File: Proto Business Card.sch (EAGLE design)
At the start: 551 parts

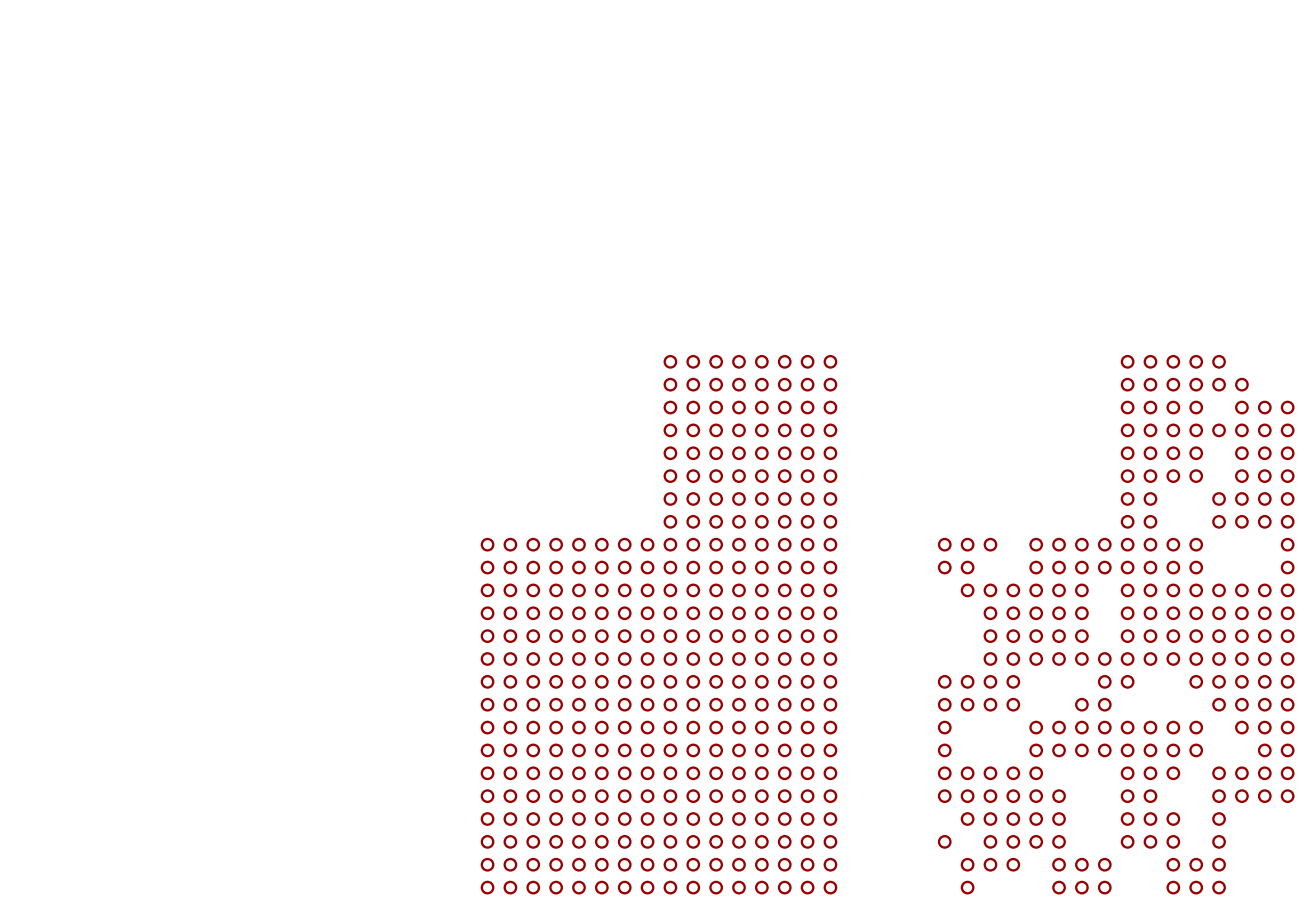
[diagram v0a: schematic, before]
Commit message: Text is now on, and the grid is complete. Still missing example layers on the back
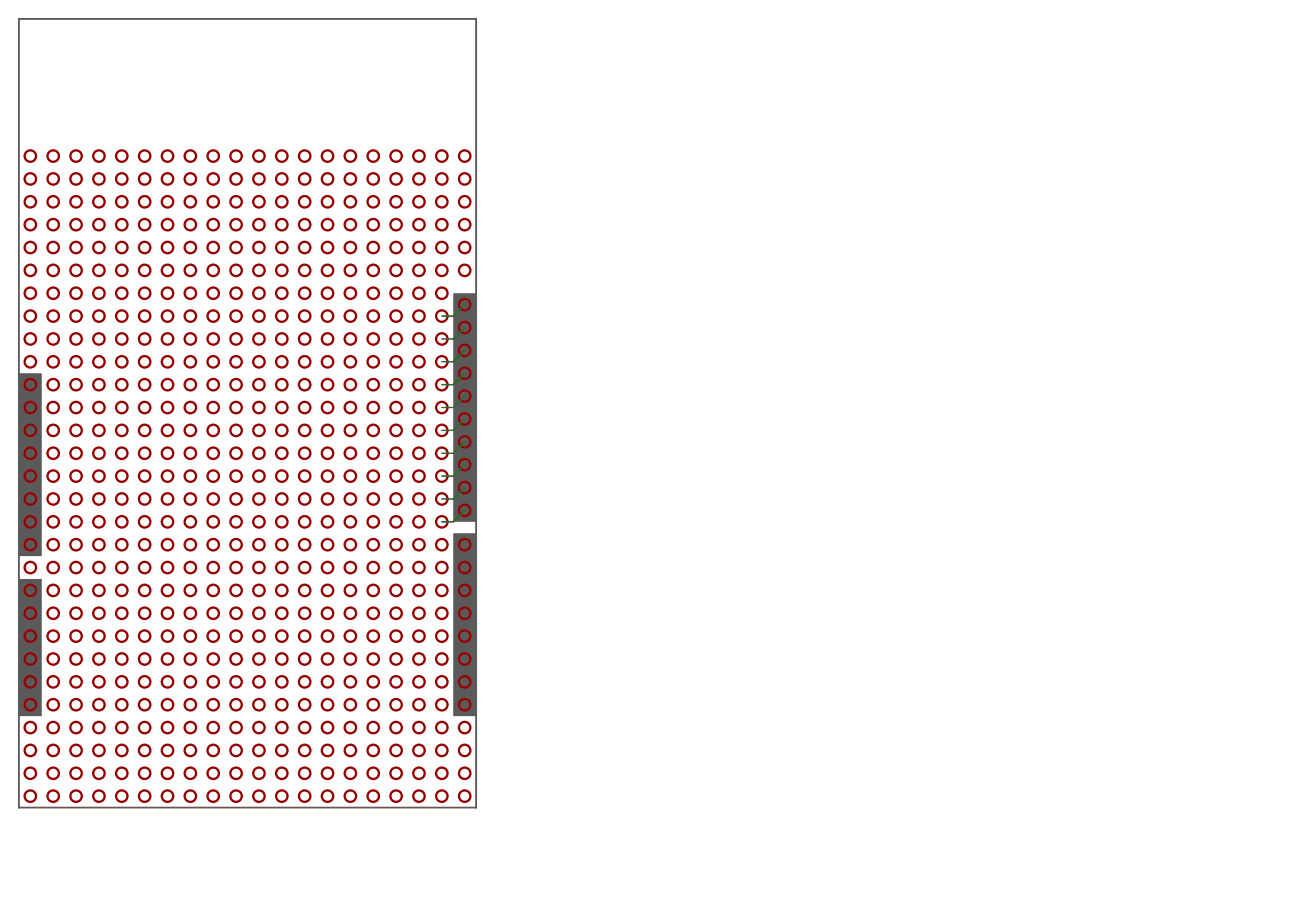
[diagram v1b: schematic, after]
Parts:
- removed U$576, U$577, U$578, U$579, U$580, U$581, U$582, U$583, U$584, U$589, U$596, U$597, U$598, U$599, U$600, U$601, U$602, U$603, U$604, U$605, U$606, U$607, U$608, U$609, U$610, U$611, U$612, U$613, U$614, U$621, U$622, U$623, U$624, U$625, U$626, U$627, U$628, U$629, U$630, U$631, U$632, U$633, U$634, U$635, U$636, U$637, U$638, U$639: VIA.4-4, flowerpad:VIA.4-4
- added U$100, U$148, U$149, U$74, U$75, U$95, U$96, U$97, U$98, U$99: VIA.NONE, flowerpad:VIA.NONE
- added U$120, U$121, U$122, U$123, U$124, U$125, U$145, U$146, U$150, U$20, U$22, U$23, U$24, U$25, U$45, U$46, U$501, U$502, U$566, U$567, U$568, U$569: VIA.3-3, flowerpad:VIA.3-3
- added U$147, U$171, U$172, U$173, U$174, U$175, U$47, U$48, U$49, U$497, U$498, U$499, U$50, U$500, U$503, U$504, U$505, U$506, U$507, U$508, U$509, U$510, U$511, U$512, U$515, U$516, U$517, U$518, U$519, U$520, U$540, U$541, U$542, U$543, U$544, U$545, U$565, U$70, U$71, U$72, U$73: VIA.4-4, flowerpad:VIA.4-4
- added U$170, U$21, U$570: VIA.2-2.CORNER, flowerpad:VIA.2-2.CORNER
- U$1, U$3, U$37, U$574, U$575: value VIA.4-4 -> VIA.2-2.CORNER; device flowerpad:VIA.4-4 -> flowerpad:VIA.2-2.CORNER
- U$10, U$11, U$112, U$113, U$12, U$13, U$14, U$15, U$152, U$153, U$16, U$17, U$18, U$182, U$183, U$19, U$2, U$211, U$212, U$240, U$241, U$26, U$269, U$27, U$270, U$28, U$29, U$298, U$299, U$30, U$31, U$32, U$327, U$328, U$33, U$34, U$35, U$356, U$357, U$36, U$385, U$386, U$4, U$414, U$415, U$443, U$444, U$472, U$473, U$5, U$530, U$531, U$559, U$560, U$571, U$572, U$573, U$588, U$6, U$7, U$77, U$78, U$8, U$9: value VIA.4-4 -> VIA.3-3; device flowerpad:VIA.4-4 -> flowerpad:VIA.3-3
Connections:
- new net N$1: U$145.VIA, U$99.VIA
- new net N$10: U$149.VIA, U$170.VIA
- new net N$2: U$100.VIA, U$146.VIA
- new net N$3: U$124.VIA, U$97.VIA
- new net N$4: U$125.VIA, U$98.VIA
- new net N$5: U$122.VIA, U$95.VIA
- new net N$6: U$123.VIA, U$96.VIA
- new net N$7: U$120.VIA, U$74.VIA
- new net N$8: U$121.VIA, U$75.VIA
- new net N$9: U$148.VIA, U$150.VIA
